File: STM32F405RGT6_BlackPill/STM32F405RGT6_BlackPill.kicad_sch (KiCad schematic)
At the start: 22 parts, among them U1 STM32F405RGTx, Y1 25Mhz

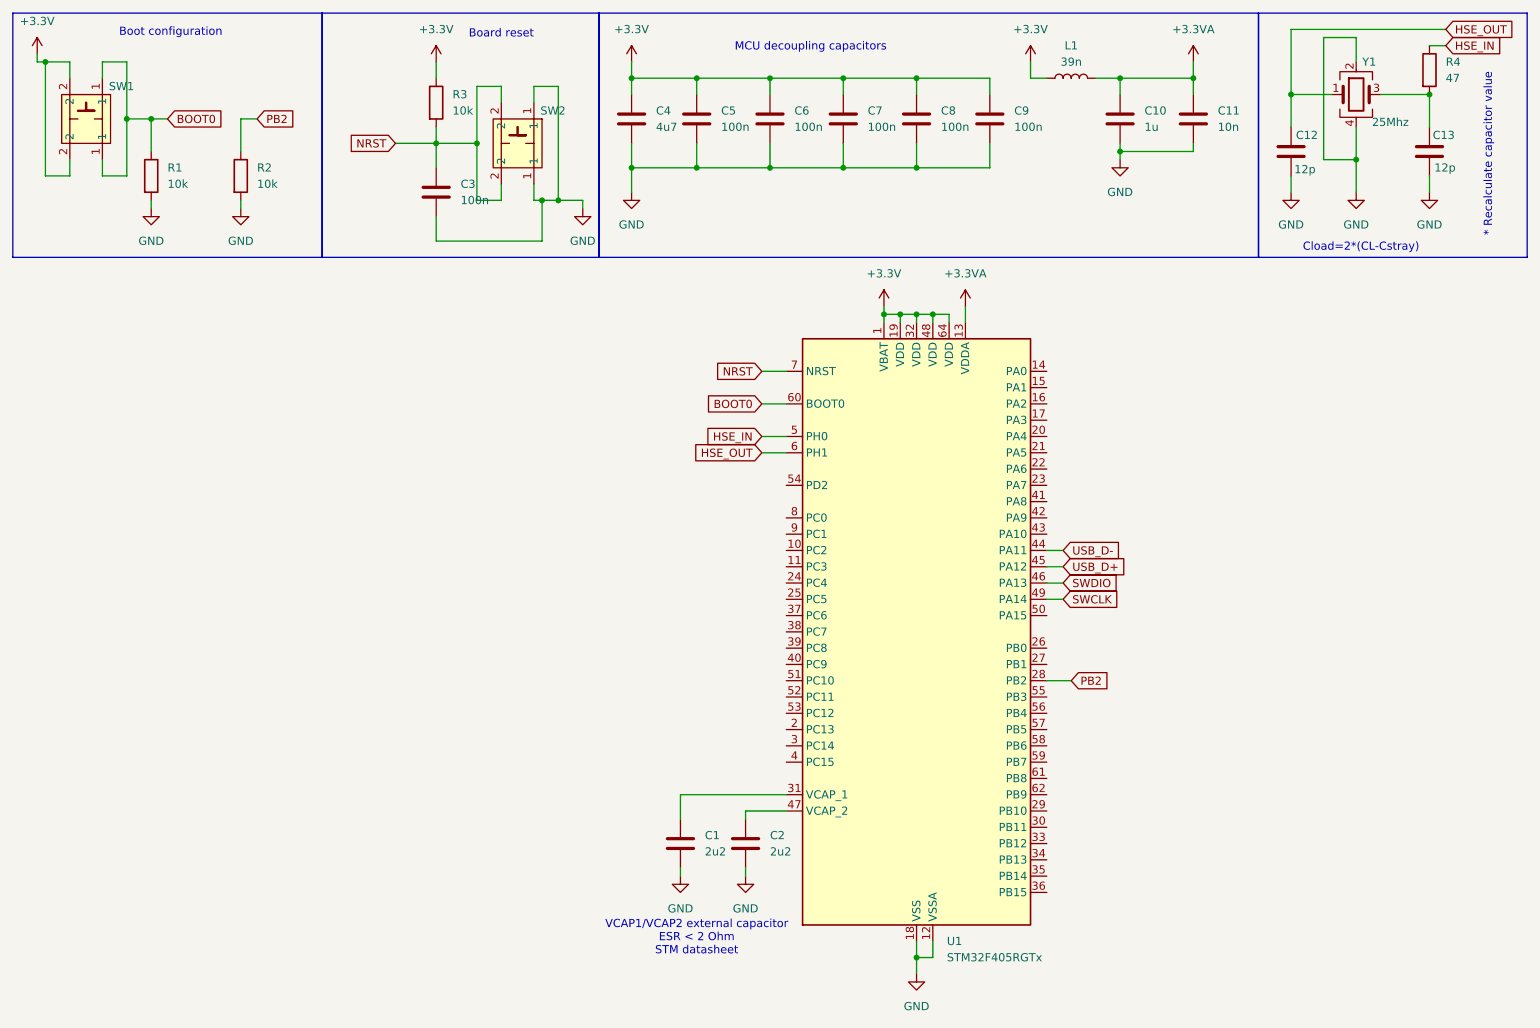
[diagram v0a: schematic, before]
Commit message: Add power and USB scheme
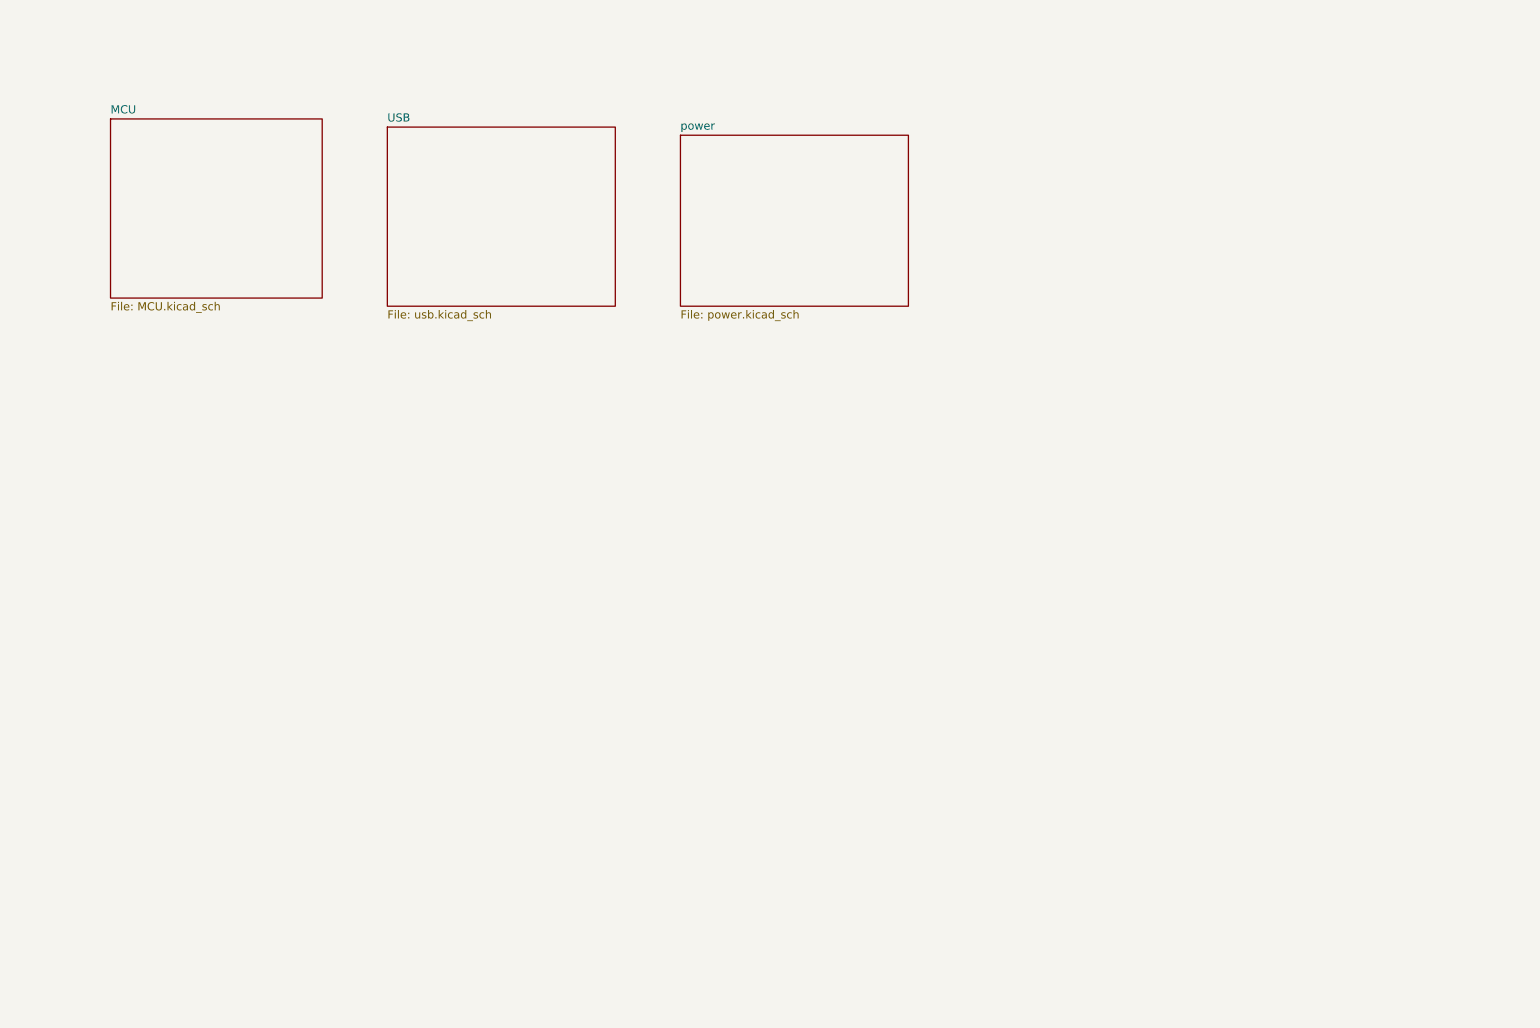
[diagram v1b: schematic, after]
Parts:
- removed C1, C2: 2u2, symbol Device:C
- removed C10: 1u, symbol Device:C
- removed C11: 10n, symbol Device:C
- removed C12, C13: 12p, symbol Device:C
- removed C3, C5, C6, C7, C8, C9: 100n, symbol Device:C
- removed C4: 4u7, symbol Device:C
- removed L1: 39n, symbol Device:L
- removed R1, R2, R3: 10k, symbol Device:R
- removed R4: 47, symbol Device:R
- removed SW1, SW2: ~, symbol BlackPillLibrary:SW_PUSH_6mm_H5mm
- removed U1: STM32F405RGTx, Package_CSP:ST_WLCSP-90_Die413, symbol MCU_ST_STM32F4:STM32F405RGTx
- removed Y1: 25Mhz, symbol Device:Crystal_GND24
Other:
- added sheet MCU (MCU.kicad_sch)
- added sheet USB (usb.kicad_sch)
- added sheet power (power.kicad_sch)
- note removed: "* Recalculate capacitor value"
- note removed: "Board reset"
- note removed: "Boot configuration"
- note removed: "Cload=2*(CL-Cstray)"
- note removed: "MCU decoupling capacitors"
- note removed: "VCAP1/VCAP2 external capacitor ESR < 2 Ohm STM datasheet"
